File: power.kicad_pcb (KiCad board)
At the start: 4 copper layers, 11 parts, among them J6 Conn_01x02, U7 SGM40561

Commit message: Build power board
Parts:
- removed R1: R, Resistors_SMD:R_0805
- added J7: Conn_01x05, Pin_Headers:Pin_Header_Straight_1x05_Pitch2.54mm, F.Cu at (120.0, 93.1)
- added Q2: FDC6420C, TO_SOT_Packages_SMD:SuperSOT-6, F.Cu at (124.3, 97.2)
- added U5: SGM2036_UTDFN, TO_SOT_Packages_SMD:SOT-23-5, F.Cu at (129.3, 96.7)
- U7: footprint Housings_DFN_QFN:VDFN-8-1EP_2x2mm_Pitch0.5mm -> Housings_DFN_QFN:TDFN-2x2-8L
- moved C6 19.1 mm to (128.6, 92.2)
- moved R4 16.5 mm to (125.0, 92.9), turned to 270 degrees
- moved R5 15.2 mm to (122.8, 92.9), turned to 270 degrees
- moved R6 13.0 mm to (129.3, 103.8)
- moved C3 12.0 mm to (124.4, 100.9)
- moved D1 11.8 mm to (133.8, 93.6), turned to 180 degrees
- moved R7 11.2 mm to (129.3, 101.7)
- moved U7 8.01 mm to (124.5, 103.4), turned to 270 degrees
- moved C7 7.10 mm to (129.2, 99.7)
- moved J6 5.80 mm to (134.0, 99.9), turned to 270 degrees
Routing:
- net Net-(C7-Pad1): track 0.00 -> 30.0 mm
- net VIN: track 0.00 -> 21.7 mm
- net PPR: track 0.00 -> 19.2 mm, vias 0 -> 1
- net +3.3V: track 0.00 -> 18.4 mm, vias 0 -> 2
- net CHG: track 0.00 -> 15.5 mm
- net (GND): track 0.00 -> 13.7 mm, vias 0 -> 7
- net +5: track 0.00 -> 13.2 mm
- net Net-(R7-Pad1): track 0.00 -> 3.43 mm
- net Net-(R6-Pad1): track 0.00 -> 2.92 mm
- added copper zone on B.Cu, net (GND)
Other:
- board outline added: 19.6 x 14.7 mm
- copper layers 4 -> 2
- rule solder_mask_min_width: 0.25 -> 0.101

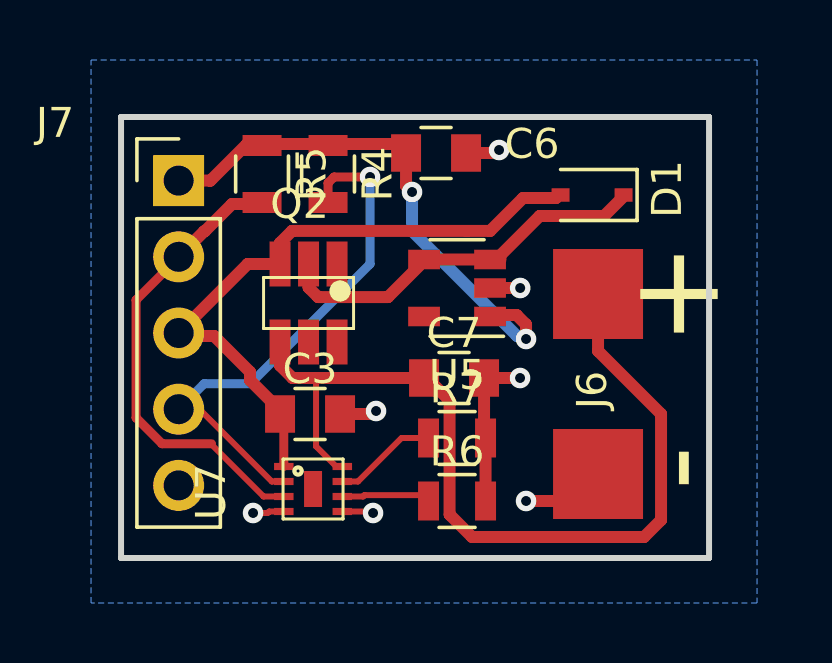
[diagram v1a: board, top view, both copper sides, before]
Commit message: More power board layout
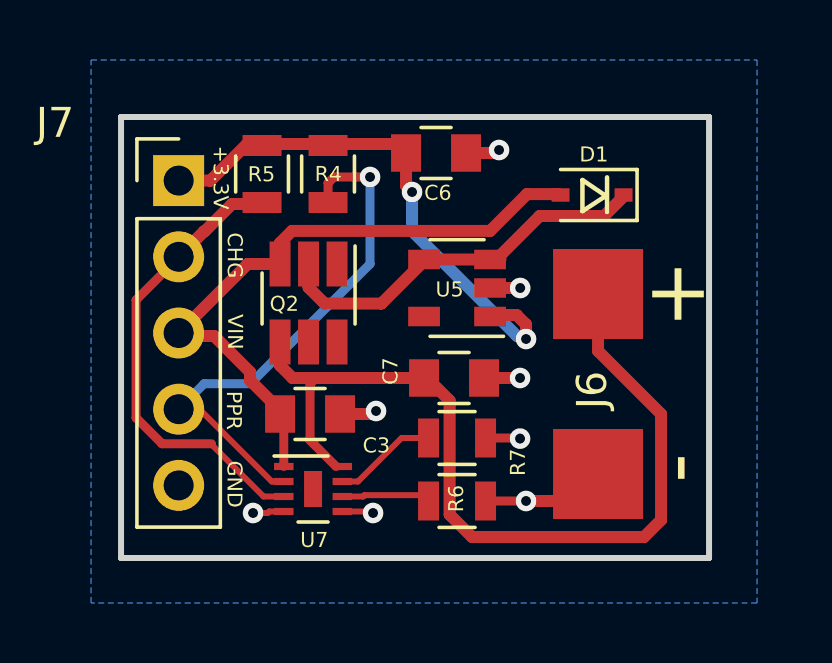
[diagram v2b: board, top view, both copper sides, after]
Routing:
- net (GND): track 13.7 -> 12.4 mm, vias 7 -> 8
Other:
- board text added: "+3.3V"
- board text added: "CHG"
- board text added: "GND"
- board text added: "PPR"
- board text added: "VIN"

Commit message: v.01 power board PCB
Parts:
- removed J7: Conn_01x05, Pin_Headers:Pin_Header_Straight_1x05_Pitch2.54mm
- removed Q2: FDC6420C, TO_SOT_Packages_SMD:SuperSOT-6
- added C9: 10uF, Capacitors_SMD:C_0805_HandSoldering, F.Cu at (136.6, 103.8)
- added D2: GREEN, LEDs:LED_0805, F.Cu at (146.6, 106.3)
- added P1: BATT, my-fp-library:Battery Pads 3x3, F.Cu at (146.3, 103.2)
- added R14: 100K, Resistors_SMD:R_0805_HandSoldering, F.Cu at (140.4, 103.8)
- added R15: 1K, Resistors_SMD:R_0805_HandSoldering, F.Cu at (138.4, 103.7)
- added R16: 10K, Resistors_SMD:R_0805_HandSoldering, F.Cu at (141.2, 112.7)
- C3, C7: value 1uF -> 470pF
- C6: value 0.1uF -> 470pF
- D1: value ZLLS410 -> ORANGE; footprint Diodes_SMD:D_SOD-323 -> LEDs:LED_0805
- J6: value Conn_01x02 -> CONN_01X05; footprint my-fp-library:Battery Pads 3x3 -> Pin_Headers:Pin_Header_Straight_1x05_Pitch1.27mm
- R4, R5: value 100K -> 1K; footprint Resistors_SMD:R_0805 -> Resistors_SMD:R_0805_HandSoldering
- R6: value 3M -> 270K; footprint Resistors_SMD:R_0805 -> Resistors_SMD:R_0805_HandSoldering
- R7: value 301K -> 100K; footprint Resistors_SMD:R_0805 -> Resistors_SMD:R_0805_HandSoldering
- U5: value SGM2036_UTDFN -> MIC5219-3.3YM5
- U7: value SGM40561 -> MCP73871-xxI_ML; footprint Housings_DFN_QFN:TDFN-2x2-8L -> Housings_DFN_QFN:QFN-20-1EP_4x4mm_Pitch0.5mm
- moved R5 30.9 mm to (147.0, 112.1), turned to 180 degrees
- moved R4 28.0 mm to (147.0, 110.2), turned to 180 degrees
- moved D1 19.3 mm to (146.6, 108.2)
- moved C6 15.6 mm to (133.7, 106.9)
- moved U7 15.0 mm to (138.4, 108.9), turned to 90 degrees
- moved R7 12.7 mm to (135.7, 112.7)
- moved C3 12.2 mm to (133.7, 108.8)
- moved U5 11.0 mm to (129.8, 107.7), turned to 0 degrees
- moved R6 7.87 mm to (133.0, 110.8)
- moved C7 5.25 mm to (129.6, 104.9), turned to 180 degrees
- moved J6 5.11 mm to (129.6, 102.4), turned to 90 degrees
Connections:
- C3 pad 1: VIN -> Net-(C3-Pad1)
- C7 pad 1: Net-(C7-Pad1) -> +3.3V
- D1 pad 1: +5 -> Net-(D1-Pad1)
- D1 pad 2: VIN -> VBUS
- J6 pad 1: Net-(C7-Pad1) -> (GND)
- J6 pad 2: (GND) -> PWR_SENSE
- R4 pad 1: +3.3V -> Net-(D1-Pad1)
- R4 pad 2: PPR -> PWR_SENSE
- R5 pad 1: +3.3V -> Net-(D2-Pad1)
- R5 pad 2: CHG -> STAT
- R6 pad 1: Net-(R6-Pad1) -> VBUS
- R6 pad 2: (GND) -> Net-(R6-Pad2)
- R7 pad 1: Net-(R7-Pad1) -> Net-(R6-Pad2)
- U5 pad 1: +3.3V -> +5
- U5 pad 4: +5 -> Net-(C3-Pad1)
- U5 pad 5: (no net) -> +3.3V
- U7 pad 1: VIN -> +5
- U7 pad 2: PPR -> Net-(R6-Pad2)
- U7 pad 3: CHG -> VBUS
- U7 pad 4: (GND) -> VBUS
- U7 pad 5: (GND) -> Net-(R16-Pad1)
- U7 pad 6: Net-(R6-Pad1) -> (no net)
- U7 pad 7: Net-(R7-Pad1) -> STAT
- U7 pad 8: Net-(C7-Pad1) -> PWR_SENSE
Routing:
- net PWR_SENSE: track 0.00 -> 48.6 mm, vias 0 -> 2
- net VBUS: track 0.00 -> 33.8 mm, vias 0 -> 4
- net STAT: track 0.00 -> 30.5 mm
- net Net-(C7-Pad1): track 30.1 -> 0.00 mm
- net VIN: track 21.7 -> 0.00 mm
- net PPR: track 19.2 -> 0.00 mm, vias 1 -> 0
- net CHG: track 15.5 -> 0.00 mm
- net Net-(C9-Pad1): track 0.00 -> 13.8 mm
- net +3.3V: track 18.4 -> 6.93 mm, vias 2 -> 1
- net (GND): track 12.4 -> 2.37 mm, vias 8 -> 11
- net Net-(D2-Pad1): track 0.00 -> 8.18 mm
- net Net-(R6-Pad2): track 0.00 -> 6.39 mm
- net Net-(R7-Pad1): track 3.43 -> 0.00 mm
- net Net-(U7-Pad21): track 0.00 -> 3.37 mm, vias 0 -> 4
- net Net-(R6-Pad1): track 2.92 -> 0.00 mm
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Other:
- board size 19.6 x 14.7 mm -> 23.9 x 13.6 mm
- board text added: "PWR"
- board text added: "STAT"
- board text added: "VBUS"
- board text added: "v0.1"
- board text removed: "CHG"
- board text removed: "PPR"
- board text removed: "VIN"

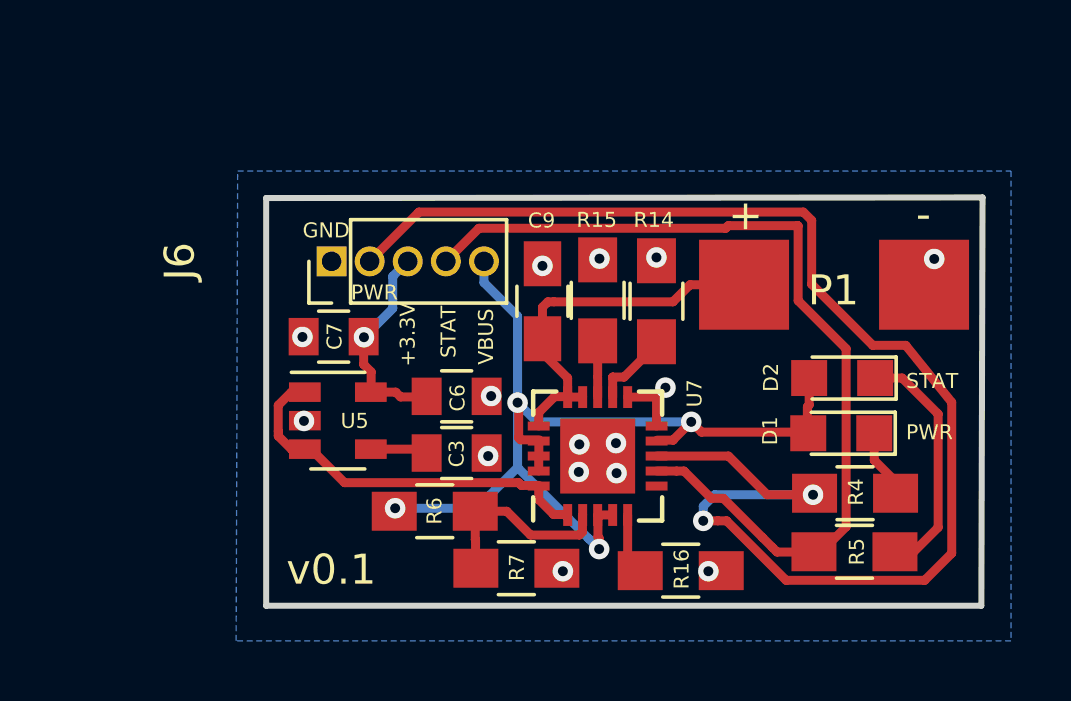
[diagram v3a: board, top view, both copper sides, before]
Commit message: update for power footprint
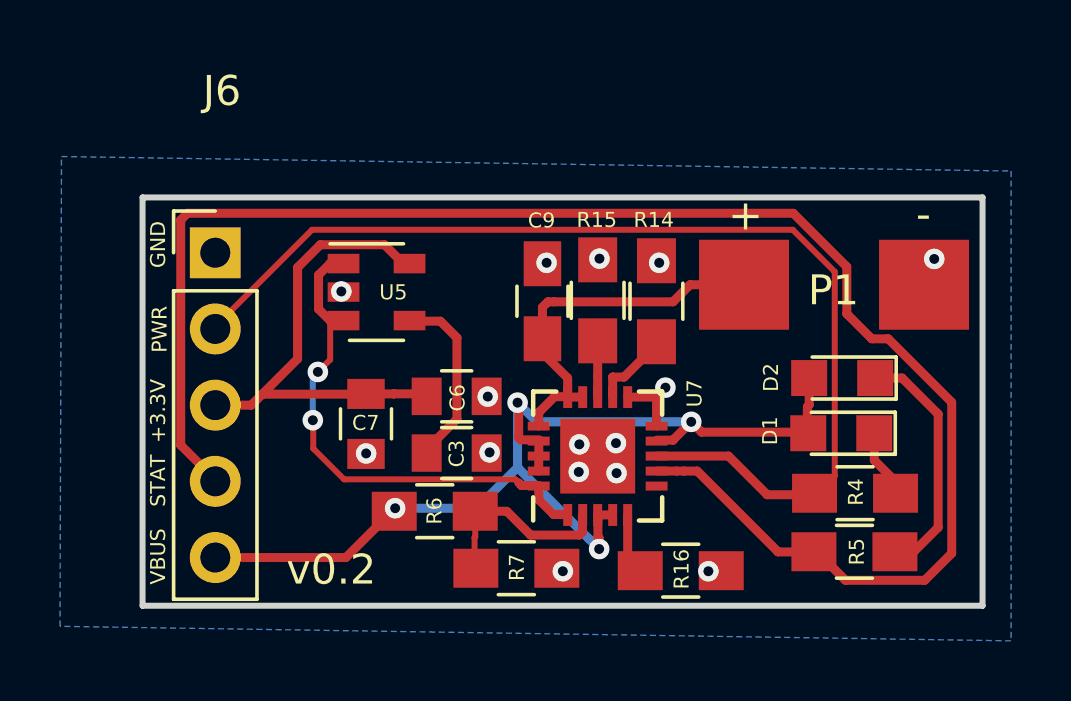
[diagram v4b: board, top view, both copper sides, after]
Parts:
- J6: footprint Pin_Headers:Pin_Header_Straight_1x05_Pitch1.27mm -> Pin_Headers:Pin_Header_Straight_1x05_Pitch2.54mm
- moved U5 4.48 mm to (131.1, 103.4)
- moved J6 3.89 mm to (125.7, 102.1), turned to 0 degrees
- moved C7 3.10 mm to (130.7, 107.8), turned to 270 degrees
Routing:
- net STAT: track 30.5 -> 55.1 mm
- net PWR_SENSE: track 48.6 -> 36.1 mm, vias 2 -> 0
- net +3.3V: track 6.93 -> 16.1 mm, vias 1 -> 0
- net Net-(C3-Pad1): track 1.93 -> 6.30 mm
- net +5: track 13.1 -> 17.4 mm, vias 0 -> 2
- net VBUS: track 33.8 -> 35.3 mm
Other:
- board size 23.9 x 13.6 mm -> 28 x 13.6 mm
- board text added: "v0.2"
- board text removed: "v0.1"

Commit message: More layout changes
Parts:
- removed D1: ORANGE, LEDs:LED_0805
- removed D2: GREEN, LEDs:LED_0805
- removed J6: CONN_01X05, Pin_Headers:Pin_Header_Straight_1x05_Pitch2.54mm
- removed P1: BATT, my-fp-library:Battery Pads 3x3
- removed R5: 1K, Resistors_SMD:R_0805_HandSoldering
- removed U5: MIC5219-3.3YM5, TO_SOT_Packages_SMD:SOT-23-5
- removed U7: MCP73871-xxI_ML, Housings_DFN_QFN:QFN-20-1EP_4x4mm_Pitch0.5mm
- added C13: 4.7uF, Capacitors_SMD:C_0603_HandSoldering, F.Cu at (139.0, 77.5)
- added J3: Conn_01x05, Pin_Headers:Pin_Header_Straight_1x05_Pitch2.54mm, F.Cu at (150.6, 88.0)
- added TP2: TestPoint, Measurement_Points:Measurement_Point_Square-SMD-Pad_Big, F.Cu at (147.9, 76.2)
- added TP4: TestPoint BATT GND, Measurement_Points:Measurement_Point_Square-SMD-Pad_Big, F.Cu at (143.4, 76.1)
- added U3: MCP73871-xxI_ML, Housings_DFN_QFN:QFN-20-1EP_4x4mm_Pitch0.5mm, F.Cu at (142.2, 81.8)
- added U4: MIC5219-3.3YM5, TO_SOT_Packages_SMD:SOT-23-5, F.Cu at (154.2, 82.5)
- C3: value 470pF -> 10uF; footprint Capacitors_SMD:C_0805 -> Capacitors_SMD:C_0603_HandSoldering
- C6, C7: footprint Capacitors_SMD:C_0805 -> Capacitors_SMD:C_0603_HandSoldering
- C9: value 10uF -> 470pF; footprint Capacitors_SMD:C_0805_HandSoldering -> Capacitors_SMD:C_0603_HandSoldering
- R14, R15, R16, R6, R7: footprint Resistors_SMD:R_0805_HandSoldering -> Resistors_SMD:R_0603_HandSoldering
- R4: value 1K -> 10K; footprint Resistors_SMD:R_0805_HandSoldering -> Resistors_SMD:R_0603_HandSoldering
- moved C7 38.2 mm to (156.6, 79.8), turned to 0 degrees
- moved C6 33.7 mm to (157.0, 82.5), turned to 270 degrees
- moved C3 31.4 mm to (146.8, 80.2)
- moved R6 30.9 mm to (136.7, 80.0)
- moved R7 30.9 mm to (136.7, 81.8), turned to 180 degrees
- moved C9 30.5 mm to (158.5, 82.5), turned to 270 degrees
- moved R16 29.4 mm to (136.7, 83.7), turned to 180 degrees
- moved R4 25.0 mm to (143.8, 85.4), turned to 0 degrees
- moved R15 23.6 mm to (146.9, 81.8), turned to 0 degrees
- moved R14 21.5 mm to (146.9, 83.3), turned to 0 degrees
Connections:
- C3 pad 1: Net-(C3-Pad1) -> /BATT
- C6 pad 1: +3.3V -> Net-(C6-Pad1)
- C7 pad 1: +3.3V -> +3.3
- C9 pad 1: Net-(C9-Pad1) -> +3.3
- R4 pad 1: Net-(D1-Pad1) -> +5
- R4 pad 2: PWR_SENSE -> /PWR_CHRGING
- R6 pad 1: VBUS -> +5
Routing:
- net STAT: track 55.1 -> 0.00 mm
- net +5: track 17.4 -> 56.4 mm
- net PWR_SENSE: track 36.1 -> 0.00 mm
- net VBUS: track 35.3 -> 0.00 mm, vias 4 -> 0
- net /VOUT: track 0.00 -> 22.3 mm, vias 0 -> 2
- net /PWR_CHRGING: track 0.00 -> 18.4 mm, vias 0 -> 2
- net /BATT: track 0.00 -> 16.9 mm, vias 0 -> 2
- net +3.3V: track 16.1 -> 0.00 mm
- net Net-(C9-Pad1): track 13.8 -> 0.00 mm
- net (GND): track 2.37 -> 15.8 mm, vias 11 -> 16
- net Net-(D2-Pad1): track 8.18 -> 0.00 mm
- net Net-(C3-Pad1): track 6.30 -> 0.00 mm
- net Net-(U3-Pad21): track 0.00 -> 3.75 mm
- net Net-(U7-Pad21): track 3.37 -> 0.00 mm, vias 4 -> 0
- net Net-(C6-Pad1): track 0.00 -> 2.65 mm
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- added copper zone on F.Cu, net +3.3
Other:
- board size 28 x 13.6 mm -> 35.5 x 16.3 mm
- board text added: "+5v"
- board text added: "BAT+"
- board text added: "CHRG"
- board text added: "v0.3"
- board text removed: "PWR"
- board text removed: "STAT"
- board text removed: "VBUS"
- board text removed: "v0.2"
